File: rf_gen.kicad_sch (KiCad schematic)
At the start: 52 parts, among them J1 Conn_01x07_Male, J2 Screw_Terminal_01x04, J3 Conn_01x05_Male, Q1 GS61004B, Q2 G3R350MT12J, U1 NPC81074, U2 AP62150

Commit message: Finishing touches
Fixed design violations. Had to make exceptions for 1kV due to the dimensions of the parts
Added top and front views of PCB
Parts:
- rf_out1: footprint Connector_Coaxial:SMA_Molex_73251-1153_EdgeMount_Horizontal -> Connector_Coaxial:SMA_Amphenol_132289_EdgeMount
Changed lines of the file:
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@@
       (effects (font (size 1.27 1.27)) (justify left))
     )
-    (property "Footprint" "Connector_Coaxial:SMA_Molex_73251-1153_EdgeMount_Horizontal" (id 2) (at 270.51 74.93 0)
+    (property "Footprint" "Connector_Coaxial:SMA_Amphenol_132289_EdgeMount" (id 2) (at 270.51 74.93 0)
       (effects (font (size 1.27 1.27)) hide)
     )
@@
     )
     (path "/129f78c6-46f2-4b09-95be-d1628639933d"
-      (reference "rf_out1") (unit 1) (value "Conn_Coaxial") (footprint "Connector_Coaxial:SMA_Molex_73251-1153_EdgeMount_Horizontal")
-    )
-  )
+      (reference "rf_out1") (unit 1) (value "Conn_Coaxial") (footprint "Connector_Coaxial:SMA_Amphenol_132289_EdgeMount")
+    )
+  )

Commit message: Added 3d model for toroid inductor
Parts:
- L2: footprint Inductor_THT:L_Toroid_Vertical_L10.0mm_W5.0mm_P5.08mm -> rf_gen:L_Toroid_Vertical_L10.0mm_W5.0mm_P5.08mm
- rf_out1: footprint Connector_Coaxial:SMA_Amphenol_132289_EdgeMount -> rf_gen:SMA_EdgeMount
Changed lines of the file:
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@@
       (effects (font (size 1.27 1.27)) (justify left))
     )
-    (property "Footprint" "Connector_Coaxial:SMA_Amphenol_132289_EdgeMount" (id 2) (at 270.51 74.93 0)
+    (property "Footprint" "rf_gen:SMA_EdgeMount" (id 2) (at 270.51 74.93 0)
       (effects (font (size 1.27 1.27)) hide)
     )
@@
     (property "Reference" "L2" (id 0) (at 71.12 73.66 90))
     (property "Value" "650n" (id 1) (at 71.12 76.2 90))
-    (property "Footprint" "Inductor_THT:L_Toroid_Vertical_L10.0mm_W5.0mm_P5.08mm" (id 2) (at 71.12 80.01 0)
+    (property "Footprint" "rf_gen:L_Toroid_Vertical_L10.0mm_W5.0mm_P5.08mm" (id 2) (at 71.12 80.01 0)
       (effects (font (size 1.27 1.27)) hide)
     )
@@
     )
     (path "/6a1137d1-c355-4245-a3a5-ebc0c4cb3a36"
-      (reference "L2") (unit 1) (value "650n") (footprint "Inductor_THT:L_Toroid_Vertical_L10.0mm_W5.0mm_P5.08mm")
+      (reference "L2") (unit 1) (value "650n") (footprint "rf_gen:L_Toroid_Vertical_L10.0mm_W5.0mm_P5.08mm")
     )
     (path "/08e754a9-7ecc-42a3-9f67-8eb2bed20bd7"
@@
     )
     (path "/129f78c6-46f2-4b09-95be-d1628639933d"
-      (reference "rf_out1") (unit 1) (value "Conn_Coaxial") (footprint "Connector_Coaxial:SMA_Amphenol_132289_EdgeMount")
-    )
-  )
+      (reference "rf_out1") (unit 1) (value "Conn_Coaxial") (footprint "rf_gen:SMA_EdgeMount")
+    )
+  )

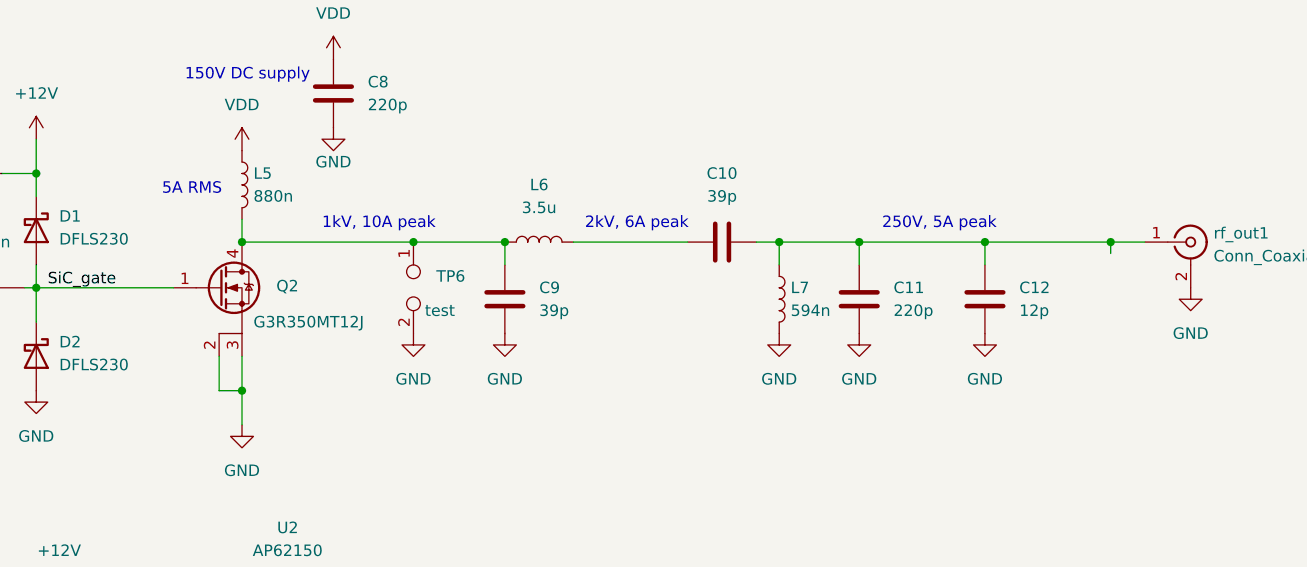
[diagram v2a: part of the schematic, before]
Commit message: Changed output filter to handle lower impedance
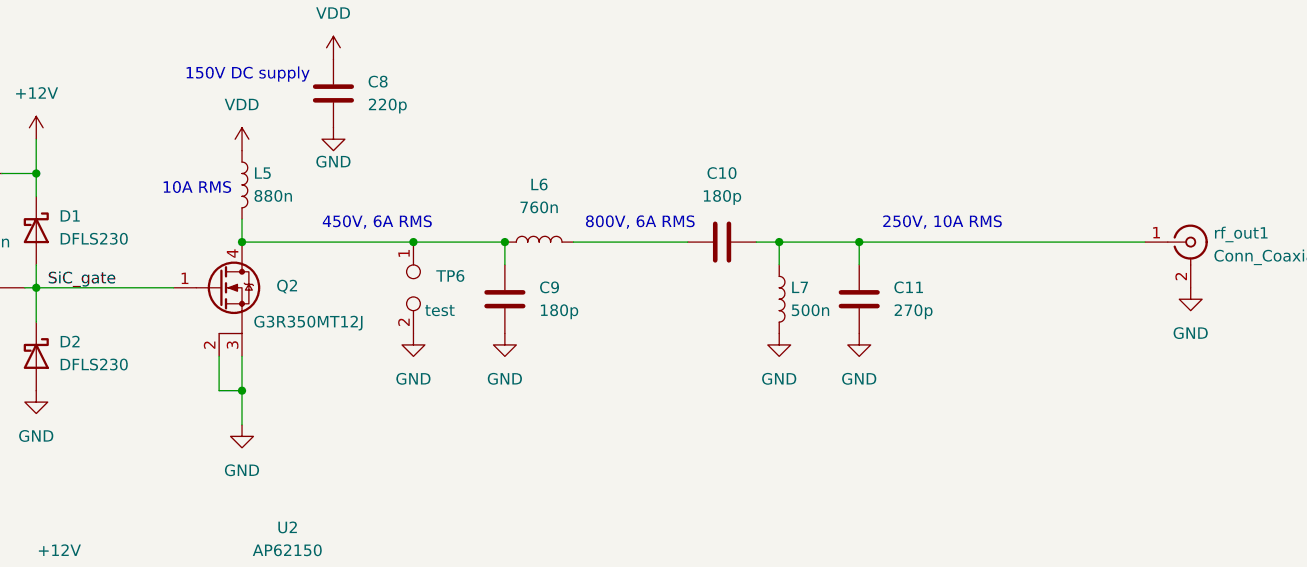
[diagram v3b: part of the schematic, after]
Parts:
- removed C12: 12p, rf_gen:C_1111_2828Metric, symbol Device:C
- C10, C9: value 39p -> 180p
- C11: value 220p -> 270p
- L6: value 3.5u -> 760n
- L7: value 594n -> 500n
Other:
- note added: "10A RMS"
- note added: "250V, 10A RMS"
- note added: "450V, 6A RMS"
- note added: "800V, 6A RMS"
- note removed: "1kV, 10A peak"
- note removed: "250V, 5A peak"
- note removed: "2kV, 6A peak"
- note removed: "5A RMS"
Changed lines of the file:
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@@
   (junction (at 165.1 74.93) (diameter 0) (color 0 0 0 0)
   )
-  (junction (at 247.65 74.93) (diameter 0) (color 0 0 0 0)
-  )
   (junction (at 187.96 121.92) (diameter 0) (color 0 0 0 0)
   )
@@
   (junction (at 224.79 74.93) (diameter 0) (color 0 0 0 0)
   )
-  (junction (at 261.62 74.93) (diameter 0) (color 0 0 0 0)
-  )
   (junction (at 67.31 80.01) (diameter 0) (color 0 0 0 0)
   )
@@
   (junction (at 144.78 127) (diameter 0) (color 0 0 0 0)
   )
+  (junction (at 222.25 121.92) (diameter 0) (color 0 0 0 0)
+  )
   (junction (at 233.68 74.93) (diameter 0) (color 0 0 0 0)
-  )
-  (junction (at 222.25 121.92) (diameter 0) (color 0 0 0 0)
   )
   (junction (at 99.06 80.01) (diameter 0) (color 0 0 0 0)
@@
     (stroke (width 0) (type default) (color 0 0 0 0))
   )
-  (wire (pts (xy 261.62 76.2) (xy 261.62 74.93))
-    (stroke (width 0) (type default) (color 0 0 0 0))
-  )
   (wire (pts (xy 46.99 142.24) (xy 46.99 143.51))
     (stroke (width 0) (type default) (color 0 0 0 0))
@@
     (stroke (width 0) (type default) (color 0 0 0 0))
   )
-  (wire (pts (xy 233.68 74.93) (xy 247.65 74.93))
-    (stroke (width 0) (type default) (color 0 0 0 0))
-  )
   (wire (pts (xy 46.99 132.08) (xy 46.99 134.62))
     (stroke (width 0) (type default) (color 0 0 0 0))
@@
     (stroke (width 0) (type default) (color 0 0 0 0))
   )
-  (wire (pts (xy 261.62 74.93) (xy 265.43 74.93))
-    (stroke (width 0) (type default) (color 0 0 0 0))
-  )
   (wire (pts (xy 59.69 170.18) (xy 59.69 177.8))
     (stroke (width 0) (type default) (color 0 0 0 0))
@@
     (stroke (width 0) (type default) (color 0 0 0 0))
   )
-  (wire (pts (xy 247.65 74.93) (xy 261.62 74.93))
-    (stroke (width 0) (type default) (color 0 0 0 0))
-  )
   (wire (pts (xy 184.15 74.93) (xy 194.31 74.93))
     (stroke (width 0) (type default) (color 0 0 0 0))
@@
     (stroke (width 0) (type default) (color 0 0 0 0))
   )
+  (wire (pts (xy 233.68 74.93) (xy 265.43 74.93))
+    (stroke (width 0) (type default) (color 0 0 0 0))
+  )
   (wire (pts (xy 222.25 121.92) (xy 234.95 121.92))
     (stroke (width 0) (type default) (color 0 0 0 0))
@@
   )
   (wire (pts (xy 43.18 172.72) (xy 72.39 172.72))
-    (stroke (width 0) (type default) (color 0 0 0 0))
-  )
-  (wire (pts (xy 247.65 74.93) (xy 247.65 77.47))
     (stroke (width 0) (type default) (color 0 0 0 0))
   )
@@
     (effects (font (size 1.27 1.27)) (justify left bottom))
   )
-  (text "250V, 5A peak" (at 236.22 73.66 0)
+  (text "250V, 10A RMS" (at 236.22 73.66 0)
     (effects (font (size 1.27 1.27)) (justify left bottom))
   )
-  (text "5A RMS" (at 156.21 69.85 0)
+  (text "10A RMS" (at 156.21 69.85 0)
     (effects (font (size 1.27 1.27)) (justify left bottom))
   )
-  (text "2kV, 6A peak" (at 203.2 73.66 0)
+  (text "800V, 6A RMS" (at 203.2 73.66 0)
     (effects (font (size 1.27 1.27)) (justify left bottom))
   )
@@
     (effects (font (size 1.27 1.27)) (justify left bottom))
   )
-  (text "1kV, 10A peak" (at 173.99 73.66 0)
+  (text "450V, 6A RMS" (at 173.99 73.66 0)
     (effects (font (size 1.27 1.27)) (justify left bottom))
   )
@@
     (pin "2")
   )
-  (symbol (lib_id "Device:C") (at 247.65 81.28 0) (unit 1)
-    (in_bom yes) (on_board yes)
-    (property "Reference" "C12" (id 0) (at 251.46 80.0099 0)
-      (effects (font (size 1.27 1.27)) (justify left))
-    )
-    (property "Value" "12p" (id 1) (at 251.46 82.55 0)
-      (effects (font (size 1.27 1.27)) (justify left))
-    )
-    (property "Footprint" "rf_gen:C_1111_2828Metric" (id 2) (at 248.6152 85.09 0)
-      (effects (font (size 1.27 1.27)) hide)
-    )
-    (property "Datasheet" "~" (id 3) (at 247.65 81.28 0)
-      (effects (font (size 1.27 1.27)) hide)
-    )
-    (pin "1")
-    (pin "2")
-  )
   (symbol (lib_id "power:GND") (at 40.64 36.83 0) (unit 1)
     (in_bom yes) (on_board yes) (fields_autoplaced)
@@
     (pin "2")
   )
-  (symbol (lib_id "power:GND") (at 247.65 85.09 0) (unit 1)
-    (in_bom yes) (on_board yes) (fields_autoplaced)
-    (property "Reference" "#PWR0103" (id 0) (at 247.65 91.44 0)
-      (effects (font (size 1.27 1.27)) hide)
-    )
-    (property "Value" "GND" (id 1) (at 247.65 90.17 0))
-    (property "Footprint" "" (id 2) (at 247.65 85.09 0)
-      (effects (font (size 1.27 1.27)) hide)
-    )
-    (property "Datasheet" "" (id 3) (at 247.65 85.09 0)
-      (effects (font (size 1.27 1.27)) hide)
-    )
-    (pin "1")
-  )
   (symbol (lib_id "power:GND") (at 234.95 132.08 0) (unit 1)
     (in_bom yes) (on_board yes) (fields_autoplaced)
@@
       (effects (font (size 1.27 1.27)) (justify left))
     )
-    (property "Value" "220p" (id 1) (at 237.49 82.5499 0)
+    (property "Value" "270p" (id 1) (at 237.49 82.5499 0)
       (effects (font (size 1.27 1.27)) (justify left))
     )
@@
       (effects (font (size 1.27 1.27)) (justify left))
     )
-    (property "Value" "594n" (id 1) (at 226.06 82.5499 0)
+    (property "Value" "500n" (id 1) (at 226.06 82.5499 0)
       (effects (font (size 1.27 1.27)) (justify left))
     )
@@
       (effects (font (size 1.27 1.27)) (justify right))
     )
-    (property "Value" "39p" (id 1) (at 198.12 82.5499 0)
+    (property "Value" "180p" (id 1) (at 198.12 82.5499 0)
       (effects (font (size 1.27 1.27)) (justify right))
     )
@@
     (in_bom yes) (on_board yes) (fields_autoplaced)
     (property "Reference" "L6" (id 0) (at 198.12 68.58 90))
-    (property "Value" "3.5u" (id 1) (at 198.12 71.12 90))
+    (property "Value" "760n" (id 1) (at 198.12 71.12 90))
     (property "Footprint" "rf_gen:inductor_core_25x18" (id 2) (at 198.12 74.93 0)
       (effects (font (size 1.27 1.27)) hide)
@@
     (in_bom yes) (on_board yes) (fields_autoplaced)
     (property "Reference" "C10" (id 0) (at 218.44 67.31 90))
-    (property "Value" "39p" (id 1) (at 218.44 69.85 90))
+    (property "Value" "180p" (id 1) (at 218.44 69.85 90))
     (property "Footprint" "rf_gen:C_1111_2828Metric" (id 2) (at 222.25 73.9648 0)
       (effects (font (size 1.27 1.27)) hide)
@@
       (reference "#PWR0102") (unit 1) (value "GND") (footprint "")
     )
-    (path "/714b35c6-c878-4848-b2ab-343d3d164c2b"
-      (reference "#PWR0103") (unit 1) (value "GND") (footprint "")
-    )
     (path "/1ec8f314-6cf8-45de-b49e-e6ca470ab65e"
       (reference "#PWR0104") (unit 1) (value "GND") (footprint "")
@@
     )
     (path "/a7cccbe7-b022-491d-9f03-06ed65321108"
-      (reference "C9") (unit 1) (value "39p") (footprint "rf_gen:C_1111_2828Metric")
+      (reference "C9") (unit 1) (value "180p") (footprint "rf_gen:C_1111_2828Metric")
     )
     (path "/c9c38eb7-16cd-4173-b19b-432d1d961844"
-      (reference "C10") (unit 1) (value "39p") (footprint "rf_gen:C_1111_2828Metric")
+      (reference "C10") (unit 1) (value "180p") (footprint "rf_gen:C_1111_2828Metric")
     )
     (path "/7982c836-1324-4f85-b09d-886e449b7c61"
-      (reference "C11") (unit 1) (value "220p") (footprint "rf_gen:C_1111_2828Metric")
-    )
-    (path "/2ad48c83-1055-4c0e-8f3e-a1535ee63a62"
-      (reference "C12") (unit 1) (value "12p") (footprint "rf_gen:C_1111_2828Metric")
+      (reference "C11") (unit 1) (value "270p") (footprint "rf_gen:C_1111_2828Metric")
     )
     (path "/be646055-5f9b-4006-8850-6ea971ff69c5"
@@
     )
     (path "/c47156a3-6b4a-4036-9b78-c505d16e9fba"
-      (reference "L6") (unit 1) (value "3.5u") (footprint "rf_gen:inductor_core_25x18")
+      (reference "L6") (unit 1) (value "760n") (footprint "rf_gen:inductor_core_25x18")
     )
     (path "/7a159c21-e862-45a0-a144-a80f91e5bc31"
-      (reference "L7") (unit 1) (value "594n") (footprint "rf_gen:inductor_core_25x18")
+      (reference "L7") (unit 1) (value "500n") (footprint "rf_gen:inductor_core_25x18")
     )
     (path "/12596e45-6707-4319-9f3d-fd07bfb54475"

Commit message: Changed L2 to use CoilCraft inductor
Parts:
- C5: value 470p -> 220p
- C8: value 220p -> 270p
- L2: value 650n -> 500n
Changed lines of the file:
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@@
       (effects (font (size 1.27 1.27)) (justify right))
     )
-    (property "Value" "220p" (id 1) (at 179.07 59.6899 0)
+    (property "Value" "270p" (id 1) (at 179.07 59.6899 0)
       (effects (font (size 1.27 1.27)) (justify right))
     )
@@
     (in_bom yes) (on_board yes) (fields_autoplaced)
     (property "Reference" "L2" (id 0) (at 71.12 73.66 90))
-    (property "Value" "650n" (id 1) (at 71.12 76.2 90))
+    (property "Value" "500n" (id 1) (at 71.12 76.2 90))
     (property "Footprint" "rf_gen:L_Toroid_Vertical_L10.0mm_W5.0mm_P5.08mm" (id 2) (at 71.12 80.01 0)
       (effects (font (size 1.27 1.27)) hide)
@@
       (effects (font (size 1.27 1.27)) (justify left))
     )
-    (property "Value" "470p" (id 1) (at 88.9 88.8999 0)
+    (property "Value" "220p" (id 1) (at 88.9 88.8999 0)
       (effects (font (size 1.27 1.27)) (justify left))
     )
@@
     )
     (path "/83df784d-b1a0-4244-af68-123c900020e2"
-      (reference "C5") (unit 1) (value "470p") (footprint "Capacitor_SMD:C_1210_3225Metric")
+      (reference "C5") (unit 1) (value "220p") (footprint "Capacitor_SMD:C_1210_3225Metric")
     )
     (path "/2725da87-8e8f-4289-9ad2-00cba9dc5cd8"
@@
     )
     (path "/174a2ad3-34b9-4b14-959e-2348b19986ae"
-      (reference "C8") (unit 1) (value "220p") (footprint "rf_gen:C_1111_2828Metric")
+      (reference "C8") (unit 1) (value "270p") (footprint "rf_gen:C_1111_2828Metric")
     )
     (path "/a7cccbe7-b022-491d-9f03-06ed65321108"
@@
     )
     (path "/6a1137d1-c355-4245-a3a5-ebc0c4cb3a36"
-      (reference "L2") (unit 1) (value "650n") (footprint "rf_gen:L_Toroid_Vertical_L10.0mm_W5.0mm_P5.08mm")
+      (reference "L2") (unit 1) (value "500n") (footprint "rf_gen:L_Toroid_Vertical_L10.0mm_W5.0mm_P5.08mm")
     )
     (path "/08e754a9-7ecc-42a3-9f67-8eb2bed20bd7"

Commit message: Updated PCB due to inductor changes
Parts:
- C5: footprint Capacitor_SMD:C_1210_3225Metric -> rf_gen:C_1111_2828Metric
- L2: footprint rf_gen:L_Toroid_Vertical_L10.0mm_W5.0mm_P5.08mm -> rf_gen:2929SQ-501
- L6: footprint rf_gen:inductor_core_25x18 -> rf_gen:inductor_air_15x15
- L7: footprint rf_gen:inductor_core_25x18 -> rf_gen:2929SQ-501
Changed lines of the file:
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@@
     (property "Reference" "L2" (id 0) (at 71.12 73.66 90))
     (property "Value" "500n" (id 1) (at 71.12 76.2 90))
-    (property "Footprint" "rf_gen:L_Toroid_Vertical_L10.0mm_W5.0mm_P5.08mm" (id 2) (at 71.12 80.01 0)
+    (property "Footprint" "rf_gen:2929SQ-501" (id 2) (at 71.12 80.01 0)
       (effects (font (size 1.27 1.27)) hide)
     )
@@
       (effects (font (size 1.27 1.27)) (justify left))
     )
-    (property "Footprint" "rf_gen:inductor_core_25x18" (id 2) (at 224.79 81.28 0)
+    (property "Footprint" "rf_gen:2929SQ-501" (id 2) (at 224.79 81.28 0)
       (effects (font (size 1.27 1.27)) hide)
     )
@@
       (effects (font (size 1.27 1.27)) (justify left))
     )
-    (property "Footprint" "Capacitor_SMD:C_1210_3225Metric" (id 2) (at 86.0552 91.44 0)
+    (property "Footprint" "rf_gen:C_1111_2828Metric" (id 2) (at 86.0552 91.44 0)
       (effects (font (size 1.27 1.27)) hide)
     )
@@
     (property "Reference" "L6" (id 0) (at 198.12 68.58 90))
     (property "Value" "760n" (id 1) (at 198.12 71.12 90))
-    (property "Footprint" "rf_gen:inductor_core_25x18" (id 2) (at 198.12 74.93 0)
+    (property "Footprint" "rf_gen:inductor_air_15x15" (id 2) (at 198.12 74.93 0)
       (effects (font (size 1.27 1.27)) hide)
     )
@@
     )
     (path "/83df784d-b1a0-4244-af68-123c900020e2"
-      (reference "C5") (unit 1) (value "220p") (footprint "Capacitor_SMD:C_1210_3225Metric")
+      (reference "C5") (unit 1) (value "220p") (footprint "rf_gen:C_1111_2828Metric")
     )
     (path "/2725da87-8e8f-4289-9ad2-00cba9dc5cd8"
@@
     )
     (path "/6a1137d1-c355-4245-a3a5-ebc0c4cb3a36"
-      (reference "L2") (unit 1) (value "500n") (footprint "rf_gen:L_Toroid_Vertical_L10.0mm_W5.0mm_P5.08mm")
+      (reference "L2") (unit 1) (value "500n") (footprint "rf_gen:2929SQ-501")
     )
     (path "/08e754a9-7ecc-42a3-9f67-8eb2bed20bd7"
@@
     )
     (path "/c47156a3-6b4a-4036-9b78-c505d16e9fba"
-      (reference "L6") (unit 1) (value "760n") (footprint "rf_gen:inductor_core_25x18")
+      (reference "L6") (unit 1) (value "760n") (footprint "rf_gen:inductor_air_15x15")
     )
     (path "/7a159c21-e862-45a0-a144-a80f91e5bc31"
-      (reference "L7") (unit 1) (value "500n") (footprint "rf_gen:inductor_core_25x18")
+      (reference "L7") (unit 1) (value "500n") (footprint "rf_gen:2929SQ-501")
     )
     (path "/12596e45-6707-4319-9f3d-fd07bfb54475"
